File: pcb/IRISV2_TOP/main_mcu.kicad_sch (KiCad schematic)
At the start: 40 parts, among them IC1 ATA6561-GAQW-N, J4 Screw_Terminal_01x03, J5 Conn_02x04_Top_Bottom, U4 STM32H563VITx, Y1 25mHz 8pf, Y2 32.768kHz 12.5pF

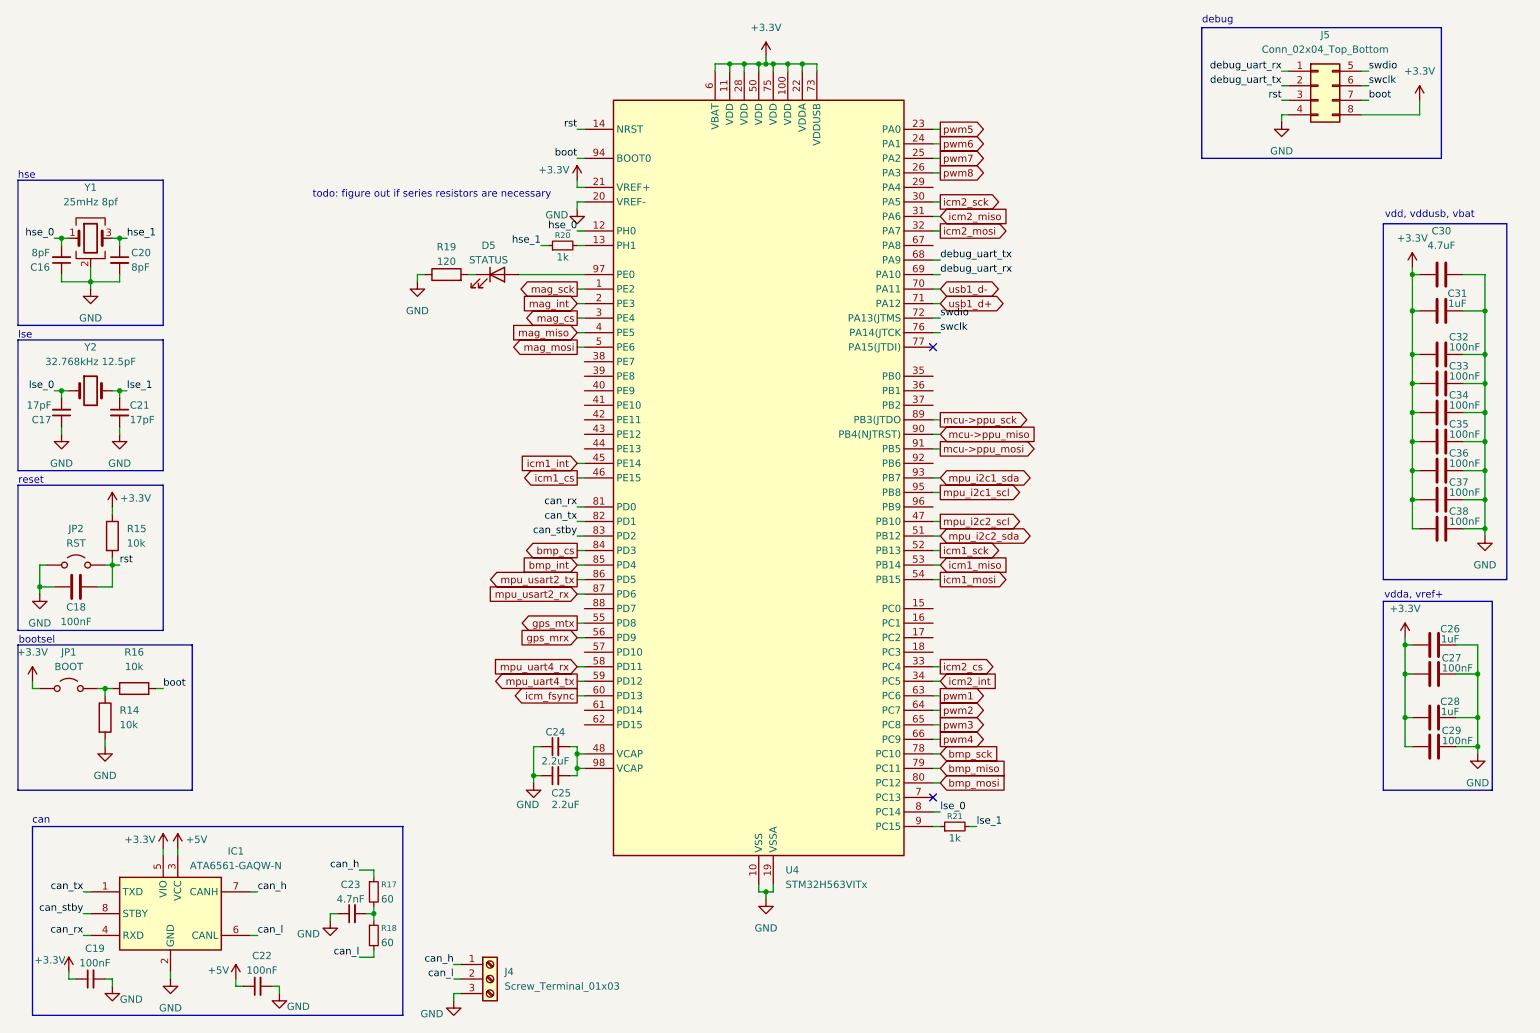
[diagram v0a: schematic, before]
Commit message: split into subprojects, fixed up stuff, started real pcb work
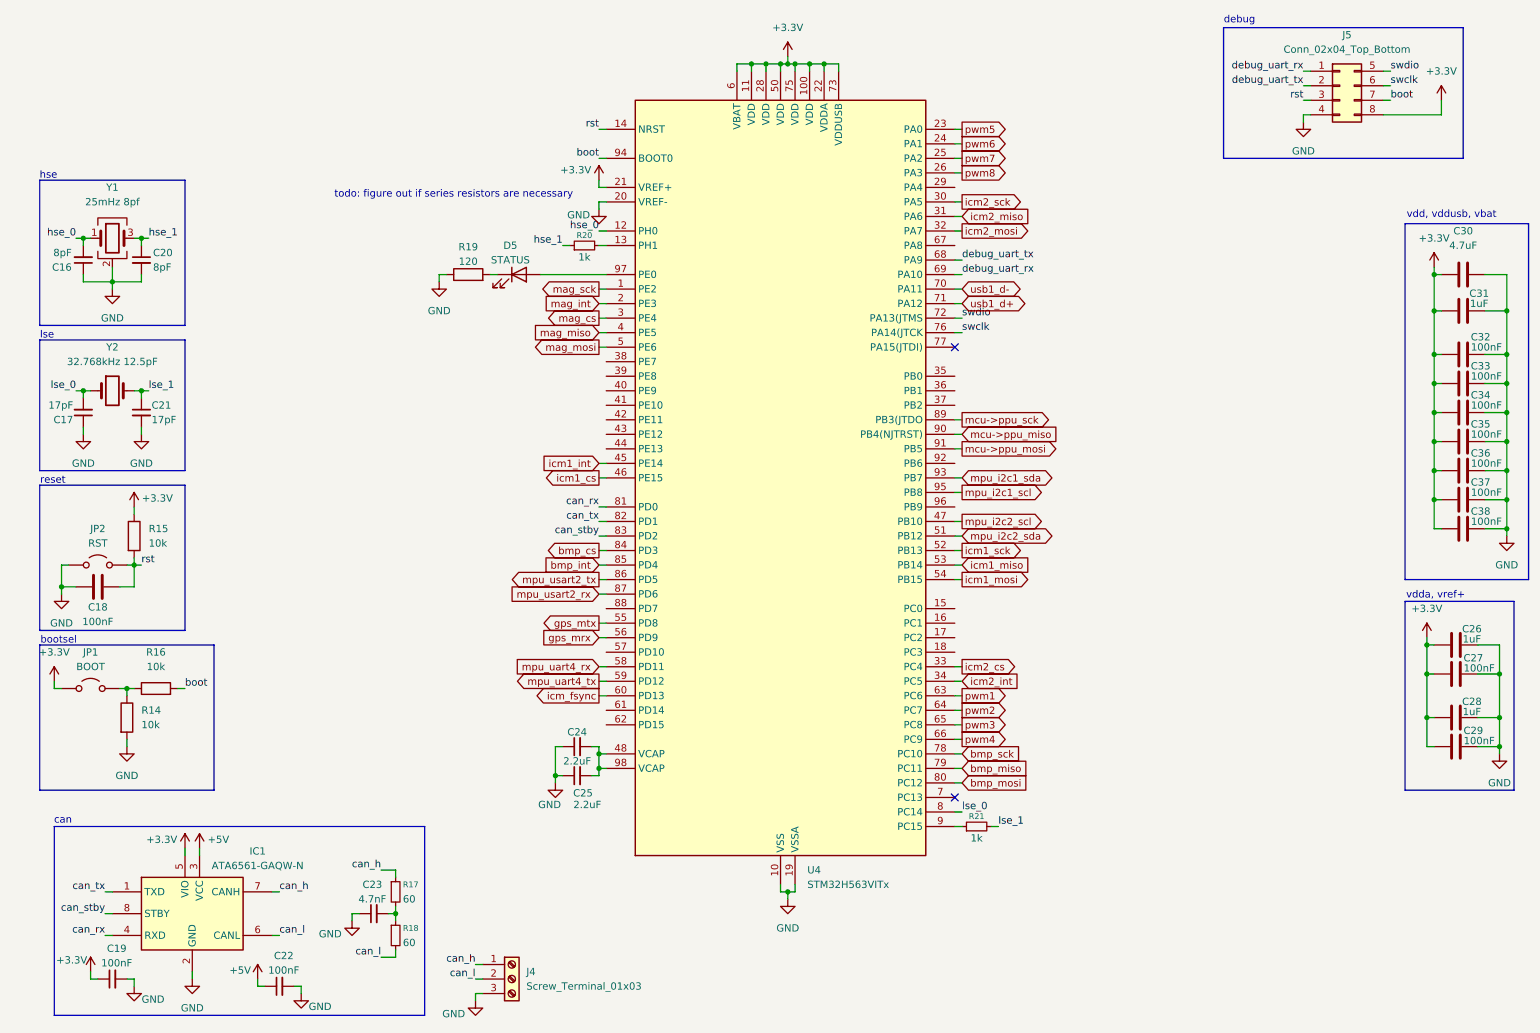
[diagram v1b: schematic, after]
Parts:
- Y1: footprint (none) -> Crystal:Crystal_SMD_3225-4Pin_3.2x2.5mm
- Y2: footprint (none) -> Crystal:Crystal_SMD_3215-2Pin_3.2x1.5mm
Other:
- moved on the sheet: C16, C17, C18, C19, C20, C21, C22, C23, C24, C25, C26, C27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

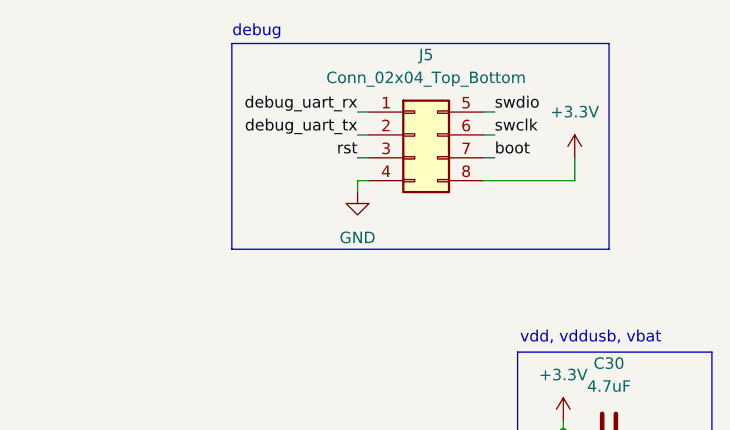
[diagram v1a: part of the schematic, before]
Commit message: gps finished minus tvs (WHY ARE THEY ALL 0201), top layout + routing started
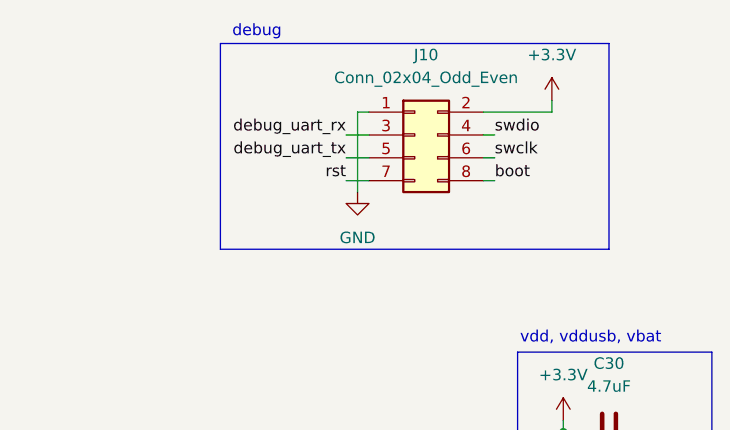
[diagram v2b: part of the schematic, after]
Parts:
- removed J5: Conn_02x04_Top_Bottom, symbol Connector_Generic:Conn_02x04_Top_Bottom
- added J10: Conn_02x04_Odd_Even, Connector_PinHeader_2.54mm:PinHeader_2x04_P2.54mm_Vertical, symbol Connector_Generic:Conn_02x04_Odd_Even
- D5: footprint (none) -> LED_SMD:LED_0805_2012Metric
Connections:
- net +3.3V: now also J10.2 (Pin_2)
- net GND: now also J10.1 (Pin_1)
- net boot: now also J10.8 (Pin_8)
- net debug_uart_rx: now also J10.3 (Pin_3)
- net debug_uart_tx: now also J10.5 (Pin_5)
- net rst: now also J10.7 (Pin_7)
- net swclk: now also J10.6 (Pin_6)
- net swdio: now also J10.4 (Pin_4)

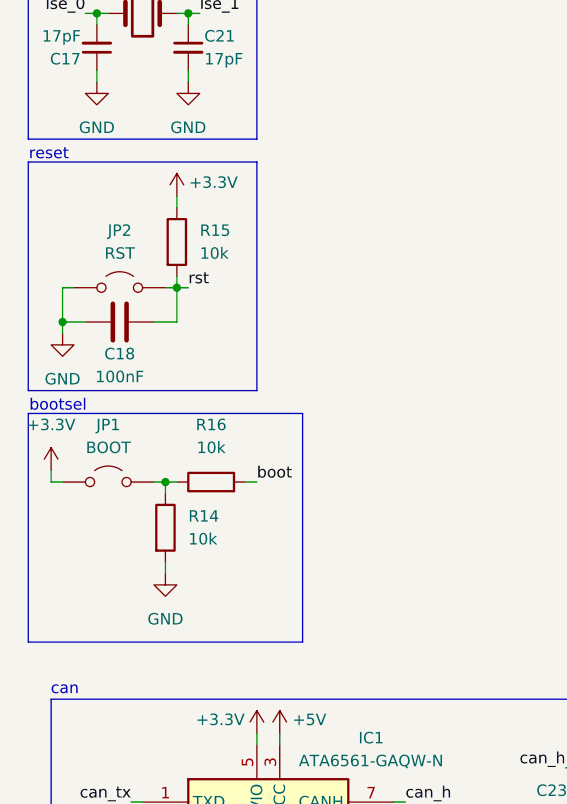
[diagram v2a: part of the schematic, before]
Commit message: removed high g accel, top board layout looking decent, routing started also - though i realized i was missing the micro sd card and that's going to be a pain to add
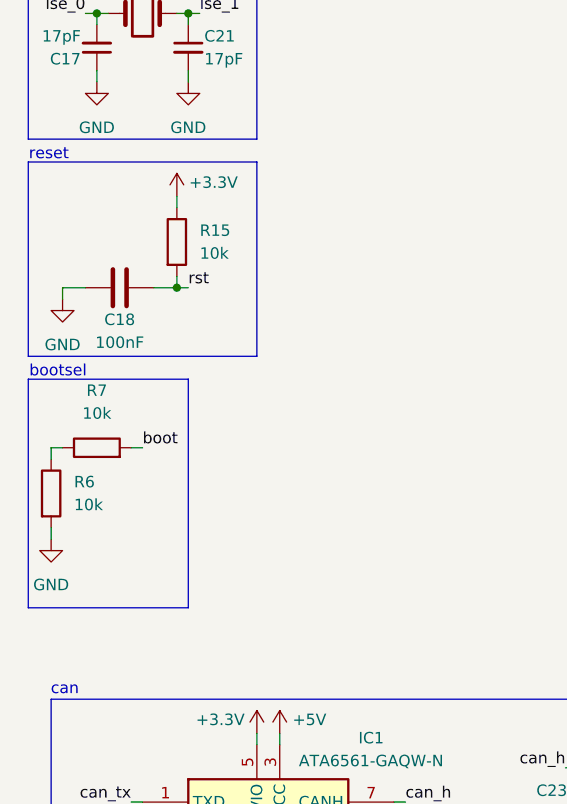
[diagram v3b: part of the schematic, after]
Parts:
- removed JP1: BOOT, TestPoint:TestPoint_2Pads_Pitch2.54mm_Drill0.8mm, symbol Jumper:Jumper_2_Open
- removed JP2: RST, TestPoint:TestPoint_2Pads_Pitch2.54mm_Drill0.8mm, symbol Jumper:Jumper_2_Open
- removed R14, R16: 10k, Resistor_SMD:R_0402_1005Metric, symbol Device:R
- added R6, R7: 10k, Resistor_SMD:R_0402_1005Metric, symbol Device:R
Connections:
- net GND: now also R6.2
- net boot: now also R7.2
- new net: R6.1, R7.1
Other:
- moved on the sheet: C18
